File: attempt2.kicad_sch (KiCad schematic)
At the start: 71 parts, among them J1 SIM_Card, J3 U.FL-R-SMT-110, J4 USB_C_Receptacle_USB2.0_14P, J5 U.FL-R-SMT-110, SW3 SW_Push, SW4 SW_Push, U1 nRF9160-SIxA, U2 TPD3F303DPVR, U3 MCP73831T-2ACI_OT, U4 MIC94092YC6-TR, U7 CP2102N-A02-GQFN24R

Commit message: Update attempt2.kicad_sch
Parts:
- BT1: symbol Device:Battery_Cell -> Connector:Conn_01x02_Pin
- R10, R2: value R -> 100k
- R11, R5: value R -> 500k
- R15: value 100k -> 22k
- R16: value 100k -> 33k
- R17: value 100k -> 1k
- R3: value 100k -> 10k
- R9: value 1M -> 10k
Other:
- moved on the sheet: BT1
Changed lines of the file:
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@@
 	(wire
 		(pts
+			(xy 115.57 388.62) (xy 115.57 394.97)
+		)
+		(stroke
+			(width 0)
+			(type default)
+		)
+	)
+	(wire
+		(pts
 			(xy 78.74 62.23) (xy 82.55 62.23)
 		)
@@
 	(wire
 		(pts
-			(xy 115.57 391.16) (xy 115.57 394.97)
+			(xy 115.57 381) (xy 115.57 386.08)
 		)
 		(stroke
@@
 	(wire
 		(pts
-			(xy 115.57 383.54) (xy 115.57 381)
-		)
-		(stroke
-			(width 0)
-			(type default)
-		)
-	)
-	(wire
-		(pts
 			(xy 351.79 313.69) (xy 351.79 314.96)
 		)
@@
 			)
 		)
-		(property "Value" "1M"
+		(property "Value" "10k"
 			(at 285.75 64.7699 0)
 			(effects
@@
 			)
 		)
-		(property "Value" "R"
+		(property "Value" "500k"
 			(at 490.22 68.5799 0)
 			(effects
@@
 			)
 		)
-		(property "Value" "100k"
+		(property "Value" "22k"
 			(at 325.12 322.5799 0)
 			(effects
@@
 			)
 		)
-		(property "Value" "R"
+		(property "Value" "100k"
 			(at 125.73 370.84 90)
 			(effects
@@
 			)
 		)
-		(property "Value" "100k"
+		(property "Value" "10k"
 			(at 488.95 160.0199 0)
 			(effects
@@
 			)
 		)
-		(property "Value" "100k"
+		(property "Value" "1k"
 			(at 248.92 71.12 90)
 			(effects
@@
 			)
 		)
-		(property "Value" "R"
+		(property "Value" "500k"
 			(at 542.29 69.8499 0)
 			(effects
@@
 			)
 		)
-		(property "Value" "100k"
+		(property "Value" "33k"
 			(at 325.12 334.0099 0)
 			(effects
@@
 			)
 		)
-		(property "Value" "R"
+		(property "Value" "100k"
 			(at 142.24 370.84 90)
 			(effects
@@
 	)
 	(symbol
-		(lib_id "Device:Battery_Cell")
-		(at 115.57 388.62 0)
+		(lib_id "Connector:Conn_01x02_Pin")
+		(at 120.65 386.08 0)
 		(mirror y)
 		(unit 1)
@@
 		(dnp no)
 		(property "Reference" "BT1"
-			(at 111.76 385.5084 0)
+			(at 114.808 386.08 0)
 			(effects
 				(font
@@
 		)
 		(property "Value" "Battery_Cell"
-			(at 111.76 388.0484 0)
+			(at 114.808 388.62 0)
 			(effects
 				(font
@@
 		)
 		(property "Footprint" "PHR_2:JST_PHR-2"
-			(at 115.57 387.096 90)
+			(at 120.65 386.08 0)
 			(effects
 				(font
@@
 		)
 		(property "Datasheet" "~"
-			(at 115.57 387.096 90)
+			(at 120.65 386.08 0)
 			(effects
 				(font
@@
 			)
 		)
-		(property "Description" "Single-cell battery"
-			(at 115.57 388.62 0)
+		(property "Description" "Generic connector, single row, 01x02, script generated"
+			(at 120.65 386.08 0)
 			(effects
 				(font

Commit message: flipped direction of usb and moved antennas to edge
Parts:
- J4: footprint Connector_USB:USB_C_Receptacle_GCT_USB4110 -> Connector_USB:USB_C_Receptacle_GCT_USB4125-xx-x-0190_6P_TopMnt_Horizontal
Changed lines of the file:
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@@
 			)
 		)
-		(property "Footprint" "Connector_USB:USB_C_Receptacle_GCT_USB4110"
+		(property "Footprint" "Connector_USB:USB_C_Receptacle_GCT_USB4125-xx-x-0190_6P_TopMnt_Horizontal"
 			(at 93.98 261.62 0)
 			(effects

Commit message: worked on erc and drc errors
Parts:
- removed C11: C, Capacitor_SMD:C_1206_3216Metric, symbol Device:C
- removed TP5, TP6: TestPoint, TestPoint:TestPoint_Pad_D2.0mm, symbol Connector:TestPoint
- added C7: 100n, Capacitor_SMD:C_1206_3216Metric, symbol Device:C
- BT1: symbol Connector:Conn_01x02_Pin -> Device:Battery_Cell
- J1: footprint Connector_Card:nanoSIM_GCT_SIM8060-6-1-14-00 -> Connector_Card:nanoSIM_GCT_SIM8060-6-0-14-00
- J4: footprint Connector_USB:USB_C_Receptacle_GCT_USB4125-xx-x-0190_6P_TopMnt_Horizontal -> Connector_USB:USB_C_Receptacle_GCT_USB4110
- R10, R2: value 100k -> R
- R11, R5: value 500k -> R
- R15: value 22k -> 100k
- R16: value 33k -> 100k
- R17: value 1k -> 100k
- R3: value 10k -> 100k
- R9: value 10k -> 1M
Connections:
- net GND: now also C7.2
- net VSYS: no longer U2.5 (VCC)
- net at U2.1 (DATA1_OUT): now also J1.2 (RST); no longer U1.43 (SIM_RST)
- net at U2.2 (CLK_OUT): now also J1.3 (CLK); no longer U1.46 (SIM_CLK)
- net at U2.3 (DATA2_OUT): now also J1.7 (I/O); no longer U1.48 (SIM_IO)
- net at U2.6 (DATA2_IN): now also U1.48 (SIM_IO); no longer J1.7 (I/O)
- net at U2.7 (CLK_IN): now also U1.46 (SIM_CLK); no longer J1.3 (CLK)
- net at U2.8 (DATA1_IN): now also U1.43 (SIM_RST); no longer J1.2 (RST)
- net at J1.1 (VCC), U1.49 (SIM_1V8): now also U2.5 (VCC), C7.1
- no-connect marks 49 -> 50
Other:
- moved on the sheet: BT1, U2

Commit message: final cleanup before design review
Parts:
- C7: value 100n -> 1n
- J4: footprint Connector_USB:USB_C_Receptacle_GCT_USB4110 -> Connector_USB:USB_C_Receptacle_GCT_USB4125-xx-x_6P_TopMnt_Horizontal
- R20: value 1.5k -> 5.1k
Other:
- note removed: "# TODO: ## bake - give mia the battery sense voltage divider values - antennae things ## mia - assign footprints :) all done except for sw pins - add notes about the expected voltage/current values for things (ie. buck/boost output, VBUS/VSYS lines, etc.) - route pcb"
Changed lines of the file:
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@@
 		)
 	)
-	(text "# TODO:\n\n## bake\n- give mia the battery sense voltage divider values\n- antennae things\n\n## mia\n- assign footprints :) \n	all done except for sw pins\n- add notes about the expected voltage/current values for things\n  (ie. buck/boost output, VBUS/VSYS lines, etc.)\n- route pcb"
-		(exclude_from_sim no)
-		(at 350.266 210.312 0)
-		(effects
-			(font
-				(size 3.81 3.81)
-			)
-			(justify left)
-		)
-	)
 	(text "GPS ANTENNA"
 		(exclude_from_sim no)
@@
 			)
 		)
-		(property "Value" "1.5k"
+		(property "Value" "5.1k"
 			(at 127 261.6199 0)
 			(effects
@@
 			)
 		)
-		(property "Value" "100n"
+		(property "Value" "1n"
 			(at 231.14 180.3399 0)
 			(effects
@@
 			)
 		)
-		(property "Footprint" "Connector_USB:USB_C_Receptacle_GCT_USB4110"
+		(property "Footprint" "Connector_USB:USB_C_Receptacle_GCT_USB4125-xx-x_6P_TopMnt_Horizontal"
 			(at 93.98 261.62 0)
 			(effects

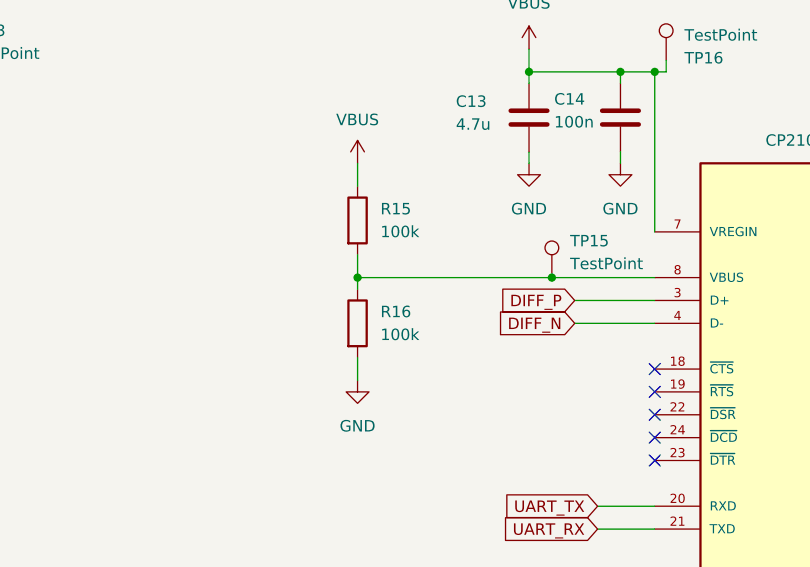
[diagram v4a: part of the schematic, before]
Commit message: voltage divider fixed
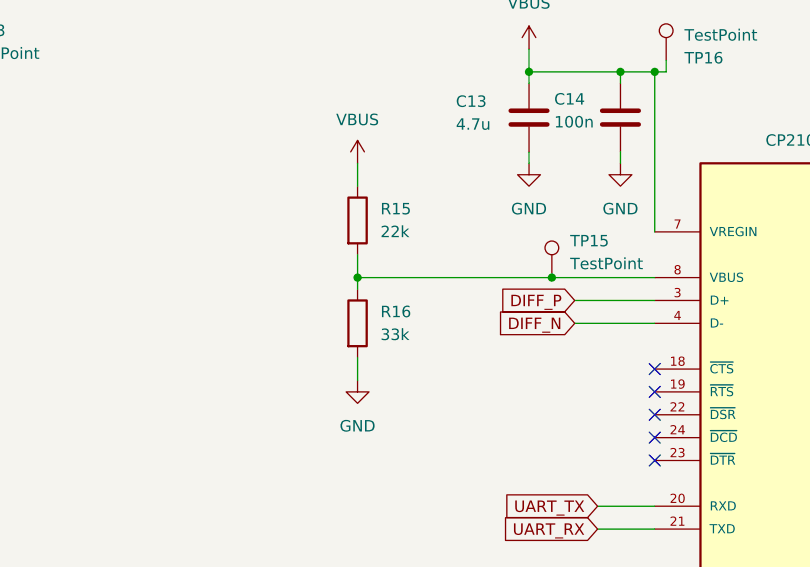
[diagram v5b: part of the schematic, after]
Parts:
- R15: value 100k -> 22k
- R16: value 100k -> 33k
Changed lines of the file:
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@@
 			)
 		)
-		(property "Value" "100k"
+		(property "Value" "22k"
 			(at 325.12 322.5799 0)
 			(effects
@@
 			)
 		)
-		(property "Value" "100k"
+		(property "Value" "33k"
 			(at 325.12 334.0099 0)
 			(effects

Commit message: FINAL BEFORE ANDREW
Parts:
- removed TP12: SWDCLK, TestPoint:TestPoint_Pad_D2.0mm, symbol Connector:TestPoint
- removed TP22: SWDIO, TestPoint:TestPoint_Pad_D2.0mm, symbol Connector:TestPoint
- added J2: Conn_01x05_Pin, Connector_PinSocket_2.54mm:PinSocket_1x05_P2.54mm_Vertical, symbol Connector:Conn_01x05_Pin
- J4: footprint Connector_USB:USB_C_Receptacle_GCT_USB4125-xx-x_6P_TopMnt_Horizontal -> Connector_USB:USB_C_Receptacle_GCT_USB4110
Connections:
- net GND: now also SW3.2, J2.3 (Pin_3); no longer SW3.1
- net VSYS: now also J2.1 (Pin_1)
- net at R17.2, U1.32 (~{RESET}): now also SW3.1, J2.5 (Pin_5); no longer SW3.2
- net at U1.33 (SWDCLK): now also J2.2 (Pin_2)
- net at U1.34 (SWDIO): now also J2.4 (Pin_4)
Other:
- note added: "1 VOLTAGE 2 CLOCK 3 GND 4 I/O 5 RESET"
- note added: "NOTES:"
- note added: "VBUS = 5.0V +-0.5v"
- note removed: "NOT EXPOSED"
- note removed: "VBUS = 5.1V +-0.5v"
- company: (none) -> Xibidi Technologies
- title: (none) -> Student Technology Against Trafficking Board
- moved on the sheet: C10, C13, C14, C15, C16, C8, C9, D1, D3, D4, JP2, L1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

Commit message: fixed resistor values
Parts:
- R10, R2: value R -> 100k
- R11, R5: value R -> 500
- R17: value 100k -> 1k
- R3: value 100k -> 4.7k
- R9: value 1M -> 10k
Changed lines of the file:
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@@
 			)
 		)
-		(property "Value" "1M"
+		(property "Value" "10k"
 			(at 285.75 64.7699 0)
 			(effects
@@
 			)
 		)
-		(property "Value" "R"
+		(property "Value" "500"
 			(at 219.71 351.7899 0)
 			(effects
@@
 			)
 		)
-		(property "Value" "R"
+		(property "Value" "100k"
 			(at 125.73 370.84 90)
 			(effects
@@
 			)
 		)
-		(property "Value" "100k"
+		(property "Value" "4.7k"
 			(at 337.82 367.0299 0)
 			(effects
@@
 			)
 		)
-		(property "Value" "100k"
+		(property "Value" "1k"
 			(at 226.0601 72.39 0)
 			(effects
@@
 			)
 		)
-		(property "Value" "R"
+		(property "Value" "500"
 			(at 271.78 353.0599 0)
 			(effects
@@
 			)
 		)
-		(property "Value" "R"
+		(property "Value" "100k"
 			(at 142.24 370.84 90)
 			(effects

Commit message: Schematic design review, remove 3.3V switcher and run right off battery, re-arrange schematic for easier reading, moved to four layer PCB because RF, cleaned up zones, including adding vbat zone. Plenty left to do, see design review notes.
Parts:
- removed C10: 100u, Capacitor_SMD:C_1206_3216Metric, symbol Device:C
- removed C8: 10u, Capacitor_SMD:C_1206_3216Metric, symbol Device:C
- removed C9: 100p, Capacitor_SMD:C_1206_3216Metric, symbol Device:C
- removed D2: SB120, Diode_THT:D_DO-41_SOD81_P10.16mm_Horizontal, symbol Diode:SB120
- removed D4: BAT20JFILM, Diode_SMD:D_2114_3652Metric, symbol BAT20JFILM:BAT20JFILM
- removed L1: 1.5u, Inductor_SMD:L_1206_3216Metric, symbol Device:L
- removed PS1: TPS63031DSKR, Package_SON:WSON-10-1EP_2.5x2.5mm_P0.5mm_EP1.2x2mm, symbol TPS63031DSKR:TPS63031DSKR
- removed R15: 22k, Resistor_SMD:R_1206_3216Metric, symbol Device:R
- removed R16: 33k, Resistor_SMD:R_1206_3216Metric, symbol Device:R
- removed R17: 1k, Resistor_SMD:R_1206_3216Metric, symbol Device:R
- removed TP13, TP14, TP8: TestPoint, TestPoint:TestPoint_Pad_D2.0mm, symbol Connector:TestPoint
- added C11: 100n, Capacitor_SMD:C_1206_3216Metric, symbol Device:C
- BT1: value Battery_Cell -> 1528-2731-ND
- R11, R5: value 500 -> 2k
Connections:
- net VBAT is gone; now on net +3V8: R10.2, TP11.1, U3.3 (VBAT)
- net GND: now also C11.2; no longer J4.S1 (SHIELD)
- net VBUS: now also TP15.1, U7.8 (VBUS)
- net at J2.5 (Pin_5), SW3.1, U1.32 (~{RESET}): now also TP3.1
- net +3V8: now reaches BT1.1 (+)
- net +3V8: now also C5.1, C6.1, J2.1 (Pin_1), JP2.2 (B), R11.1, R9.1, SW4.1, TP1.1, TP2.1, TP20.1, TP21.1, TP7.1, U1.102 (VDD1), U1.12 (VDD_GPIO), U1.22 (VDD2), U4.4 (VIN)
- removed net VSYS: C5.1, C6.1, J2.1 (Pin_1), JP2.2 (B), R11.1, R9.1, SW4.1, TP1.1, TP2.1, TP20.1, TP21.1, TP3.1, TP7.1, U1.102 (VDD1), U1.12 (VDD_GPIO), U1.22 (VDD2), U4.4 (VIN)
- new net: C11.1, J4.S1 (SHIELD)
- no-connect marks 50 -> 49
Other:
- note added: "Charge at 500 mA"
- note added: "Internal pull-up"
- note added: "MAKE SURE YOUR nRF UART IS 5V COMPLIANT"
- note added: "WARNING: Also runs load when charging"
- note removed: "1528-2731-ND"
- note removed: "BUCK BOOST"
- moved on the sheet: BT1, C1, C12, C19, C2, C3, C4, C5, C6, C7, D1, D3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
